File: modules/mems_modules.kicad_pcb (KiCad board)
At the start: 2 copper layers, 13.2 x 8.1 mm, 6 parts, among them P1 CASTELLATED_PAD, P2 CASTELLATED_PAD, P3 CASTELLATED_PAD, P4 CASTELLATED_PAD

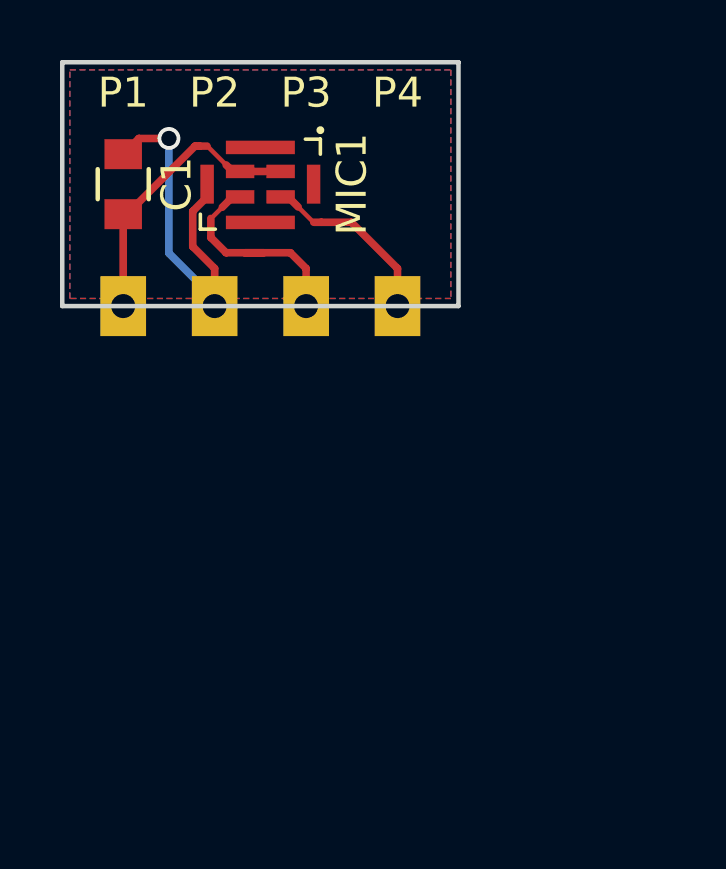
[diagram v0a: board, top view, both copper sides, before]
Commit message: Reduce MEMS mic module.
Signed-off-by: Chamon <luizchamon@gmail.com>
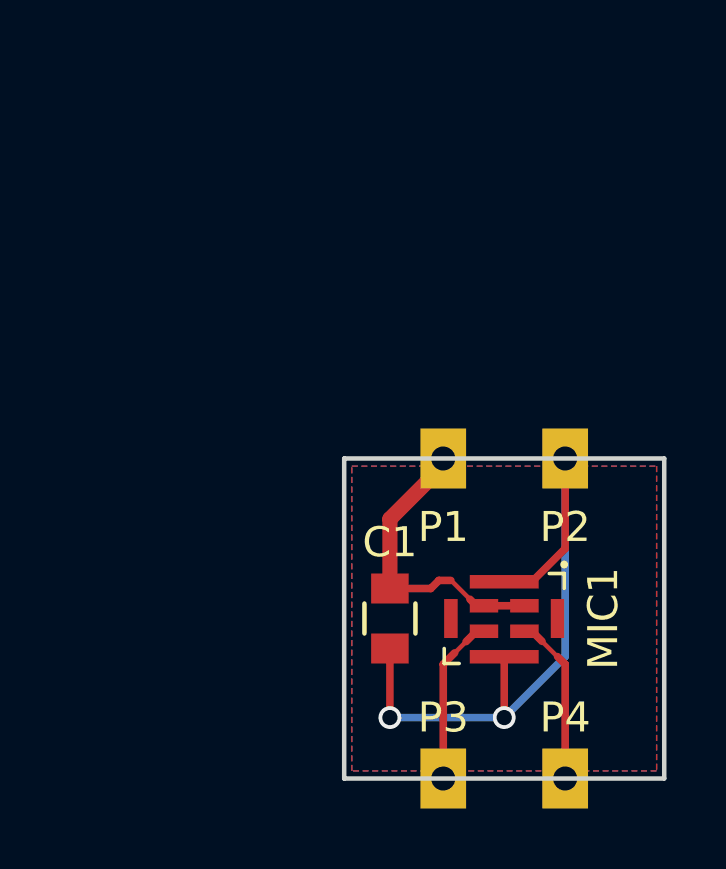
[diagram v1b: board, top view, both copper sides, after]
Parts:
- moved C1 17.0 mm to (31.2, 33.8), turned to 270 degrees
- moved P4 16.7 mm to (37.1, 39.1)
- moved MIC1 16.6 mm to (35.1, 33.8)
- moved P3 16.4 mm to (33.0, 39.1)
- moved P2 12.7 mm to (37.1, 28.4)
- moved P1 11.8 mm to (33.0, 28.4)
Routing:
- net DGND: track 12.8 -> 23.5 mm, vias 1 -> 2
- net /CLK: track 7.40 -> 5.63 mm
- net /OUT: track 6.14 -> 5.62 mm
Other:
- board size 13.2 x 8.1 mm -> 10.7 x 10.7 mm
